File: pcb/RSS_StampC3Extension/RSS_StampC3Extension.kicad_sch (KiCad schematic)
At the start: 32 parts, among them J1 5v_3Pi, J2 GND_3Pi, J5 I2C_3Pi, J6 3PI_SWTCH, J8 Conn_01x12_Pin, J9 Conn_01x10_Pin, Q1 2N7000, Q2 2N7000, Q3 BC337, Q4 TEPT4300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

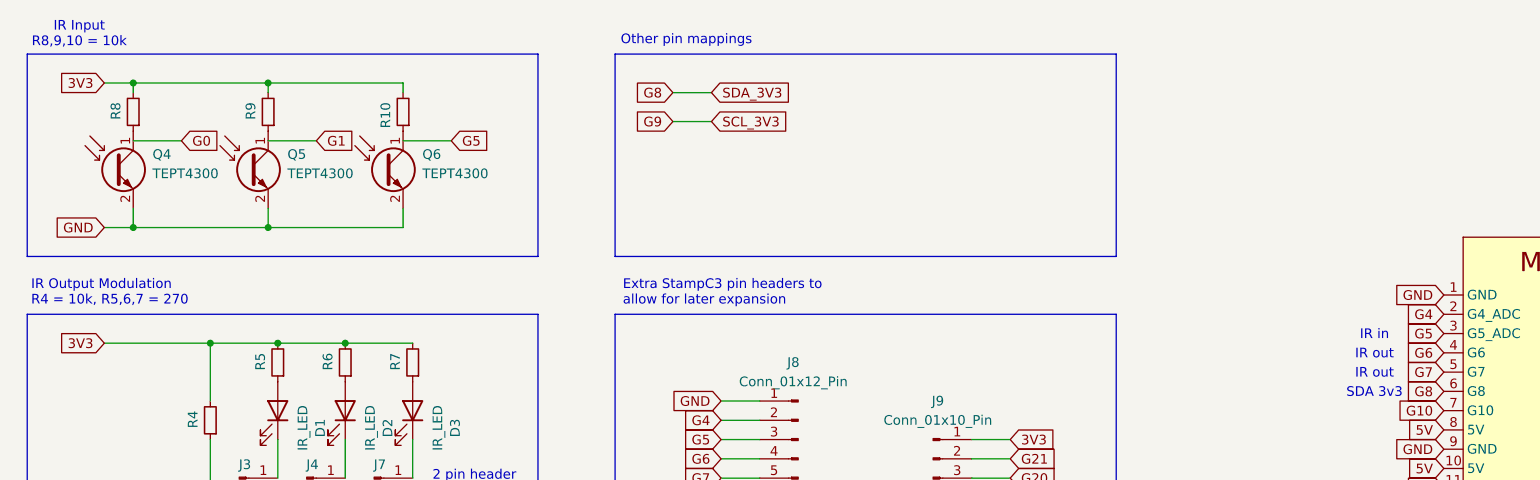
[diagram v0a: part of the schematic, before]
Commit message: Fixed missing connections between phototransistors and GPIO0,1,4 in schematic. Also, GPIO 5 cannot be used for ADC when using Wifi. So moved previous connection from GPIO 5 to 4.  Added bigger text to pcb.  Updated test code to test functionality - all working.
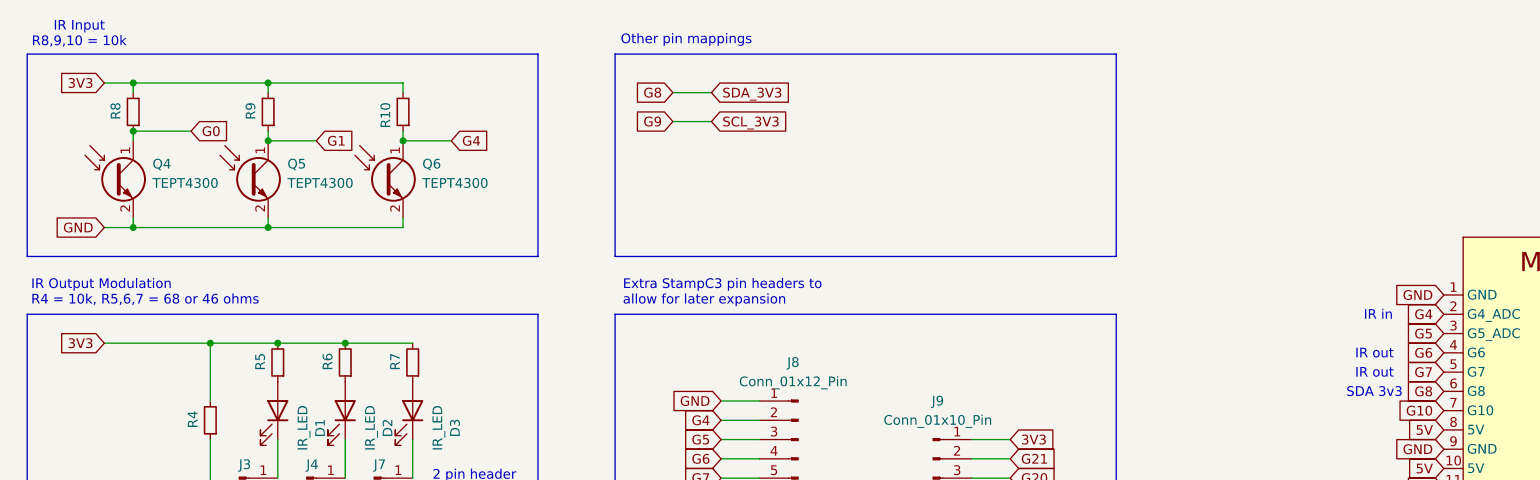
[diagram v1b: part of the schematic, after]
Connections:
- net G0: now also Q4.1 (C), R8.1
- net G1: now also Q5.1 (C), R9.1
- net G4: now also Q6.1 (C), R10.1
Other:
- note added: "IR Output Modulation R4 = 10k, R5,6,7 = 68 or 46 ohms"
- note removed: "IR Output Modulation R4 = 10k, R5,6,7 = 270"
- moved on the sheet: Q4, Q5, Q6
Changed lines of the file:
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@@
 	(text "IR in"
 		(exclude_from_sim no)
-		(at 197.866 92.964 0)
+		(at 198.374 90.424 0)
 		(effects
 			(font
@@
 		)
 	)
-	(text "IR Output Modulation\nR4 = 10k, R5,6,7 = 270"
+	(text "IR Output Modulation\nR4 = 10k, R5,6,7 = 68 or 46 ohms"
 		(exclude_from_sim no)
 		(at 20.828 89.154 0)
@@
 	)
 	(junction
+		(at 52.07 67.31)
+		(diameter 0)
+		(color 0 0 0 0)
+	)
+	(junction
 		(at 44.45 119.38)
 		(diameter 0)
@@
 	)
 	(junction
+		(at 69.85 67.31)
+		(diameter 0)
+		(color 0 0 0 0)
+	)
+	(junction
 		(at 119.38 176.53)
 		(diameter 0)
@@
 		(color 0 0 0 0)
 	)
+	(junction
+		(at 34.29 66.04)
+		(diameter 0)
+		(color 0 0 0 0)
+	)
 	(wire
 		(pts
-			(xy 34.29 67.31) (xy 40.64 67.31)
+			(xy 34.29 66.04) (xy 41.91 66.04)
 		)
 		(stroke
@@
 	(wire
 		(pts
+			(xy 52.07 67.31) (xy 58.42 67.31)
+		)
+		(stroke
+			(width 0)
+			(type default)
+		)
+	)
+	(wire
+		(pts
 			(xy 53.34 93.98) (xy 62.23 93.98)
 		)
@@
 	(wire
 		(pts
-			(xy 34.29 76.2) (xy 34.29 78.74)
+			(xy 34.29 77.47) (xy 34.29 78.74)
 		)
 		(stroke
@@
 	(wire
 		(pts
-			(xy 52.07 76.2) (xy 52.07 78.74)
+			(xy 52.07 77.47) (xy 52.07 78.74)
 		)
 		(stroke
@@
 	(wire
 		(pts
+			(xy 69.85 67.31) (xy 69.85 66.04)
+		)
+		(stroke
+			(width 0)
+			(type default)
+		)
+	)
+	(wire
+		(pts
 			(xy 38.1 186.69) (xy 38.1 190.5)
 		)
@@
 	(wire
 		(pts
-			(xy 52.07 59.69) (xy 52.07 60.96)
+			(xy 52.07 67.31) (xy 52.07 66.04)
 		)
 		(stroke
@@
 	(wire
 		(pts
-			(xy 144.78 111.76) (xy 149.86 111.76)
+			(xy 52.07 59.69) (xy 52.07 60.96)
 		)
 		(stroke
@@
 	(wire
 		(pts
-			(xy 52.07 67.31) (xy 58.42 67.31)
+			(xy 144.78 111.76) (xy 149.86 111.76)
 		)
 		(stroke
@@
 	(wire
 		(pts
-			(xy 69.85 76.2) (xy 69.85 78.74)
+			(xy 69.85 77.47) (xy 69.85 78.74)
 		)
 		(stroke
@@
 	(wire
 		(pts
+			(xy 34.29 67.31) (xy 34.29 66.04)
+		)
+		(stroke
+			(width 0)
+			(type default)
+		)
+	)
+	(wire
+		(pts
 			(xy 38.1 190.5) (xy 45.72 190.5)
 		)
@@
 		)
 	)
+	(global_label "G0"
+		(shape input)
+		(at 41.91 66.04 0)
+		(fields_autoplaced yes)
+		(effects
+			(font
+				(size 1.27 1.27)
+			)
+			(justify left)
+		)
+		(property "Intersheetrefs" "${INTERSHEET_REFS}"
+			(at 46.7205 66.04 0)
+			(effects
+				(font
+					(size 1.27 1.27)
+				)
+				(justify left)
+				(hide yes)
+			)
+		)
+	)
 	(global_label "5V"
 		(shape input)
@@
 		)
 	)
-	(global_label "G5"
+	(global_label "G4"
 		(shape input)
 		(at 76.2 67.31 0)
@@
 		)
 	)
-	(global_label "G0"
-		(shape input)
-		(at 40.64 67.31 0)
-		(fields_autoplaced yes)
-		(effects
-			(font
-				(size 1.27 1.27)
-			)
-			(justify left)
-		)
-		(property "Intersheetrefs" "${INTERSHEET_REFS}"
-			(at 45.4505 67.31 0)
-			(effects
-				(font
-					(size 1.27 1.27)
-				)
-				(justify left)
-				(hide yes)
-			)
-		)
-	)
 	(global_label "3V3"
 		(shape input)
@@
 	(symbol
 		(lib_id "Sensor_Optical:TEPT4400")
-		(at 31.75 71.12 0)
+		(at 31.75 72.39 0)
 		(unit 1)
 		(exclude_from_sim no)
@@
 		(fields_autoplaced yes)
 		(property "Reference" "Q4"
-			(at 36.83 69.1006 0)
+			(at 36.83 70.3706 0)
 			(effects
 				(font
@@
 		)
 		(property "Value" "TEPT4300"
-			(at 36.83 71.6406 0)
+			(at 36.83 72.9106 0)
 			(effects
 				(font
@@
 		)
 		(property "Footprint" "LED_THT:LED_D3.0mm_Clear"
-			(at 43.942 74.676 0)
+			(at 43.942 75.946 0)
 			(effects
 				(font
@@
 		)
 		(property "Datasheet" "https://www.vishay.com/docs/81341/tept4400.pdf"
-			(at 31.75 71.12 0)
+			(at 31.75 72.39 0)
 			(effects
 				(font
@@
 		)
 		(property "Description" "Ambient Light Sensor, NPN Epitaxial Planar Phototransistor, T-1"
-			(at 31.75 71.12 0)
+			(at 31.75 72.39 0)
 			(effects
 				(font
@@
 	(symbol
 		(lib_id "Sensor_Optical:TEPT4400")
-		(at 49.53 71.12 0)
+		(at 49.53 72.39 0)
 		(unit 1)
 		(exclude_from_sim no)
@@
 		(fields_autoplaced yes)
 		(property "Reference" "Q5"
-			(at 54.61 69.1006 0)
+			(at 54.61 70.3706 0)
 			(effects
 				(font
@@
 		)
 		(property "Value" "TEPT4300"
-			(at 54.61 71.6406 0)
+			(at 54.61 72.9106 0)
 			(effects
 				(font
@@
 		)
 		(property "Footprint" "LED_THT:LED_D3.0mm_Clear"
-			(at 61.722 74.676 0)
+			(at 61.722 75.946 0)
 			(effects
 				(font
@@
 		)
 		(property "Datasheet" "https://www.vishay.com/docs/81341/tept4400.pdf"
-			(at 49.53 71.12 0)
+			(at 49.53 72.39 0)
 			(effects
 				(font
@@
 		)
 		(property "Description" "Ambient Light Sensor, NPN Epitaxial Planar Phototransistor, T-1"
-			(at 49.53 71.12 0)
+			(at 49.53 72.39 0)
 			(effects
 				(font
@@
 	(symbol
 		(lib_id "Sensor_Optical:TEPT4400")
-		(at 67.31 71.12 0)
+		(at 67.31 72.39 0)
 		(unit 1)
 		(exclude_from_sim no)
@@
 		(fields_autoplaced yes)
 		(property "Reference" "Q6"
-			(at 72.39 69.1006 0)
+			(at 72.39 70.3706 0)
 			(effects
 				(font
@@
 		)
 		(property "Value" "TEPT4300"
-			(at 72.39 71.6406 0)
+			(at 72.39 72.9106 0)
 			(effects
 				(font
@@
 		)
 		(property "Footprint" "LED_THT:LED_D3.0mm_Clear"
-			(at 79.502 74.676 0)
+			(at 79.502 75.946 0)
 			(effects
 				(font
@@
 		)
 		(property "Datasheet" "https://www.vishay.com/docs/81341/tept4400.pdf"
-			(at 67.31 71.12 0)
+			(at 67.31 72.39 0)
 			(effects
 				(font
@@
 		)
 		(property "Description" "Ambient Light Sensor, NPN Epitaxial Planar Phototransistor, T-1"
-			(at 67.31 71.12 0)
+			(at 67.31 72.39 0)
 			(effects
 				(font

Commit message: Added a decoupling transistor, adjusted some text and added logo to silkscreen. Should be ready for production.
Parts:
- added C1: 1uf, PCM_Capacitor_THT_AKL:CP_Radial_D5.0mm_P2.00mm, symbol PCM_Capacitor_AKL:CP_Radial_D5.0mm_P2.00mm
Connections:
- net +5V: now also C1.1
- net GND: now also C1.2
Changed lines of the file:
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@@
 	(wire
 		(pts
+			(xy 78.74 168.91) (xy 78.74 171.45)
+		)
+		(stroke
+			(width 0)
+			(type default)
+		)
+	)
+	(wire
+		(pts
 			(xy 38.1 184.15) (xy 33.02 184.15)
 		)
@@
 	(wire
 		(pts
+			(xy 78.74 179.07) (xy 78.74 186.69)
+		)
+		(stroke
+			(width 0)
+			(type default)
+		)
+	)
+	(wire
+		(pts
 			(xy 144.78 119.38) (xy 149.86 119.38)
 		)
@@
 					(unit 1)
 				)
+			)
+		)
+	)
+	(symbol
+		(lib_id "PCM_Capacitor_AKL:CP_Radial_D5.0mm_P2.00mm")
+		(at 78.74 175.26 0)
+		(unit 1)
+		(exclude_from_sim no)
+		(in_bom yes)
+		(on_board yes)
+		(dnp no)
+		(property "Reference" "C1"
+			(at 82.55 173.1009 0)
+			(effects
+				(font
+					(size 1.27 1.27)
+				)
+				(justify left)
+			)
+		)
+		(property "Value" "1uf"
+			(at 82.55 175.6409 0)
+			(effects
+				(font
+					(size 1.27 1.27)
+				)
+				(justify left)
+			)
+		)
+		(property "Footprint" "PCM_Capacitor_THT_AKL:CP_Radial_D5.0mm_P2.00mm"
+			(at 78.74 185.42 0)
+			(effects
+				(font
+					(size 1.27 1.27)
+				)
+				(hide yes)
+			)
+		)
+		(property "Datasheet" "~"
+			(at 78.74 175.26 0)
+			(effects
+				(font
+					(size 1.27 1.27)
+				)
+				(hide yes)
+			)
+		)
+		(property "Description" "THT Electrolytic Capacitor, 5.0mm Diameter, 2.00mm Pitch, European Symbol, Alternate KiCad Library"
+			(at 78.74 175.26 0)
+			(effects
+				(font
+					(size 1.27 1.27)
+				)
+				(hide yes)
+			)
+		)
+		(pin "1"
+		)
+		(pin "2"
+		)
+		(instances
+			(project "RSS_StampC3Extension"
+				(path "/2ef4a934-7614-4c51-b75c-13216ab373de"
+					(reference "C1")
+					(unit 1)
+				)
